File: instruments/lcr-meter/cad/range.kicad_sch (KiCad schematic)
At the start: 21 parts, among them K1 TQ2SA-L2-5V 100R, K2 TQ2SA-L2-5V 5k, K3 TQ2SA-L2-5V 100k, Q2 AO3400A, Q3 AO3400A, Q4 AO3400A, Q5 AO3400A

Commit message: Rev E board: four-terminal BNC jacks, K4 reference relay
- J3 header -> four SAMZO BNC-KYWE-295-W4-N (C41416668, hand fit) on the
  top edge at 22 mm pitch: J3 HCUR (DUT_HI), J7 HPOT, J8 LPOT, J9 LCUR
  (DUT_LO). Followers U6.5/U7.5 now sense HPOT/LPOT. R105/R106 1k (basic
  C21190) tie POT to CUR for two-terminal leads. Board 140 x 105 mm.
- K4 TQ2SA: COM2 = HCUR, NO2 -> R107 1k 0.1 % -> LCUR; RESET on the
  shared RLY_RST, SET on Q6/GPIO14 (GPIO12's pad is boxed in by USB_SENSE).
- C78 moves onto the LCUR run. All copper hand-specified in rev_e_routes.py.
- rebuild: ERC 0, DRC 0 / 0 unconnected, parity PASS; independent_check
  620 pins, 0 findings (topology check updated for 4T).
- Five boards $453.46 (+$36.87); 5 PCBs / 2 assembled $309.31.

Co-Authored-By: Claude Opus 5.5 <noreply@anthropic.com>
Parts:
- added D9: 1N4148WS, LCR:D_SOD-323, symbol LCR:DIODE
- added K4: TQ2SA-L2-5V REF, LCR:Relay_DPDT_Panasonic_TQ2SA_SMD, symbol LCR:RELAY2L
- added Q6: AO3400A, LCR:SOT-23, symbol LCR:NMOS
- added R107: 1k 0.1%, LCR:R_0603_1608Metric, symbol LCR:R
- added R108: 100R, LCR:R_0603_1608Metric, symbol LCR:R
- added R109: 100k, LCR:R_0603_1608Metric, symbol LCR:R
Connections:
- net GND: now also Q6.2 (S), R109.2
- net RLY_RST: now also K4.6 (RST-)
- net VRLY: now also D9.1 (K), K4.1 (SET+), K4.10 (RST+)
- new net DUT_HI: K4.8 (COM2)
- new net DUT_LO: R107.1
- new net REF_A: K4.7 (NO2), R107.2
- new net RLY_SET_REF: D9.2 (A), K4.5 (SET-), Q6.3 (D)
- new net RNG_SET_REF: R108.1
- new net RNG_SET_REF_G: Q6.1 (G), R108.2, R109.1
- no-connect marks 6 -> 10
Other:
- note added: "K1 100R, K2 5k, K3 100k, K4 reference: Panasonic TQ2SA-L2-5V dual-coil latching DPDT. Pole 1: SOURCE_BUF -> RGx. Pole 2: TIA_OUT -> RFx. NC contacts unconnected. RESET coils (K1-K4) in parallel on Q2; SET coils on Q3/Q4/Q5/Q6. 1N4148WS flyback per drain. K4 reference: COM2 on HCUR, NO2 through R107 1k 0.1% to LCUR (REFCAPTURE, leads unplugged). VRLY = 5V through R101 2.2R + C112 22uF. Firmware: s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"
- note removed: "K1 100R, K2 5k, K3 100k: Panasonic TQ2SA-L2-5V dual-coil latching DPDT. Pole 1: SOURCE_BUF -> RGx. Pole 2: TIA_OUT -> RFx. NC contacts unconnected. RESET coils in parallel on Q2; SET coils on Q3/Q4/Q5. 1N4148WS flyback per drain. VRLY = 5VA through 2.2R + 22uF. Firmware: source off, RESET 20ms, SET 20ms."
- moved on the sheet: C112, R101

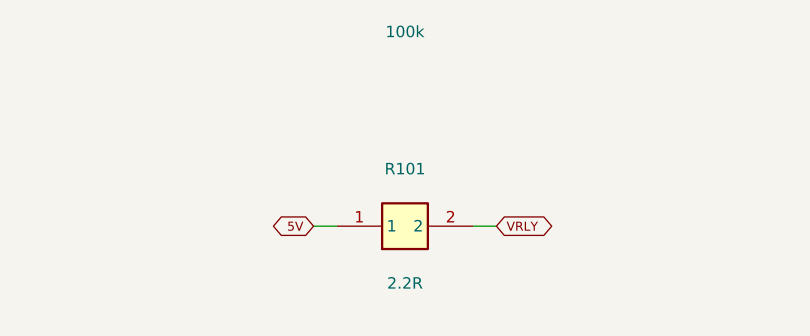
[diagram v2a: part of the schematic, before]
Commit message: lcr-meter Rev F: datasheet audit fixes (TPS65131 start-up sequencer, 5 V bulk, VREF, coil feed, test pads)
Seven independent datasheet reviews (validation/datasheet-audit-rev-f/, dispositions in its README).
One real board failure: with ENP = ENN = 3V3 both TPS65131 converters start together against
the TPS2553's 0.99 A minimum limit, and a full power-up model shows the boost can start at 5 V
= 2.1 V while U16 is still charging the node, so the board hiccups.

- U17 LM3880MF-1AA sequences ENP, then ENN 10 ms later, through open-drain flags with
  R119/R120 pull-ups to 3V3, so the EN pins never exceed VIN + 0.3 V. RC delays on the pins
  were modelled and rejected.
- C117 330 uF polymer on 5 V. R110 stays 24k: a 1.8 A limit fails the IPC-2152 rule.
- startup_surge.py: power-up from attach, 128 corners all pass, 5 V >= 3.86 V; the board
  before the audit fails 0 / 128.
- C113 4.7 uF (hot-plug), R101 1 ohm (RESET coil margin), C62 2.2 uF (TAC5112 VREF minimum
  1 uF): value-only changes.
- TP15-TP21: I2S x4 + GND, USB_VBUS + GND.
- package_cad.py now requires a placement audit for polarized caps.

Analog copper is identical to 6ae693082 (copper_delta.sh), so the extraction and stability
results carry over. ERC 0, DRC 0/0/0, JLC fab pass PASS, independent check 0 findings,
IPC-2152 0 FAIL, regulators 51 PASS / 2 FLAG. Board SHA256 780bf3ae...

Co-Authored-By: Claude Opus 5.5 <noreply@anthropic.com>
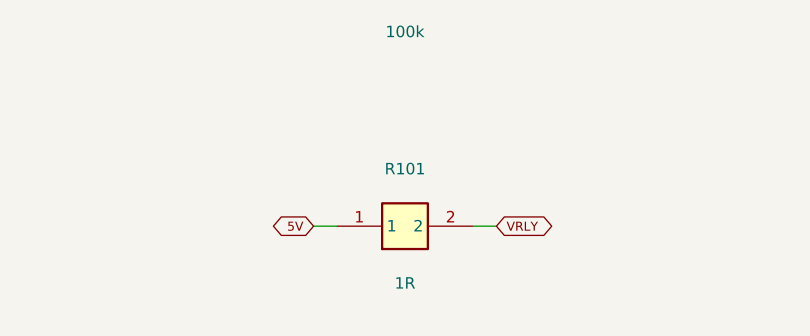
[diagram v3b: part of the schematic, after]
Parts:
- R101: value 2.2R -> 1R; LCSC C22939 -> C22936; MPN 0603WAF220KT5E -> 0603WAF100KT5E; Unit_USD 0.0034 -> 0.0027
